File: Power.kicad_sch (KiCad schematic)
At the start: 44 parts, among them SW901 PWR_SW, U901 BQ24075RGT, U902 TPS73733QDRBRQ1, U903 TPS73733QDRBRQ1

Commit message: (sch) change 2.2k R to 0402
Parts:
- R905, R908: footprint Resistor_SMD:R_0603_1608Metric_Pad0.98x0.95mm_HandSolder -> Resistor_SMD:R_0402_1005Metric; MPN RC0603FR-072K2L -> RT0402FRE072K2L
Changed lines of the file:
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@@
       (effects (font (size 1.27 1.27)))
     )
-    (property "Footprint" "Resistor_SMD:R_0603_1608Metric_Pad0.98x0.95mm_HandSolder" (at 79.375 167.64 0)
+    (property "Footprint" "Resistor_SMD:R_0402_1005Metric" (at 79.375 167.64 0)
       (effects (font (size 1.27 1.27)) hide)
     )
@@
       (effects (font (size 1.27 1.27)) hide)
     )
-    (property "MPN" "RC0603FR-072K2L" (at 79.375 167.64 0)
+    (property "MPN" "RT0402FRE072K2L" (at 79.375 167.64 0)
       (effects (font (size 1.27 1.27)) hide)
     )
@@
       (effects (font (size 1.27 1.27)) (justify left))
     )
-    (property "Footprint" "Resistor_SMD:R_0603_1608Metric_Pad0.98x0.95mm_HandSolder" (at 66.04 167.005 0)
+    (property "Footprint" "Resistor_SMD:R_0402_1005Metric" (at 66.04 167.005 0)
       (effects (font (size 1.27 1.27)) hide)
     )
@@
       (effects (font (size 1.27 1.27)) hide)
     )
-    (property "MPN" "RC0603FR-072K2L" (at 66.04 167.005 0)
+    (property "MPN" "RT0402FRE072K2L" (at 66.04 167.005 0)
       (effects (font (size 1.27 1.27)) hide)
     )

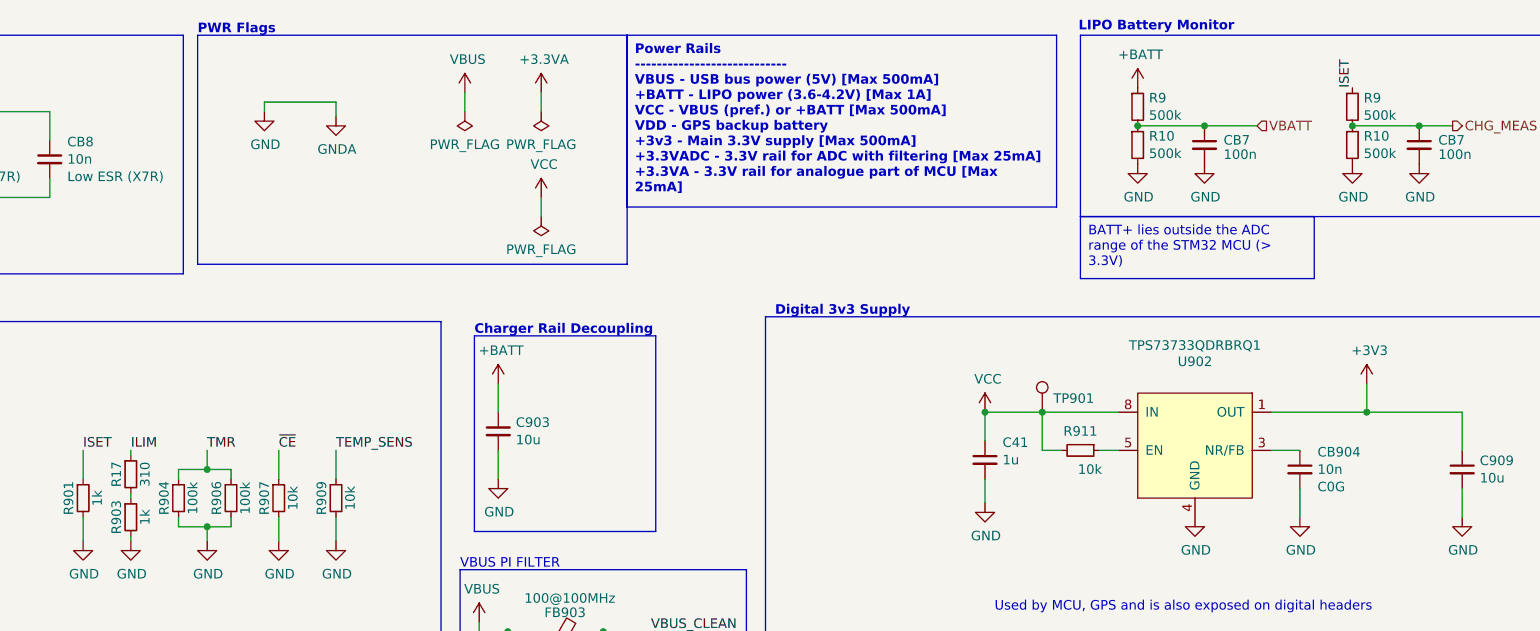
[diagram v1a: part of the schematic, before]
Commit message: (sch) change passives to 0402
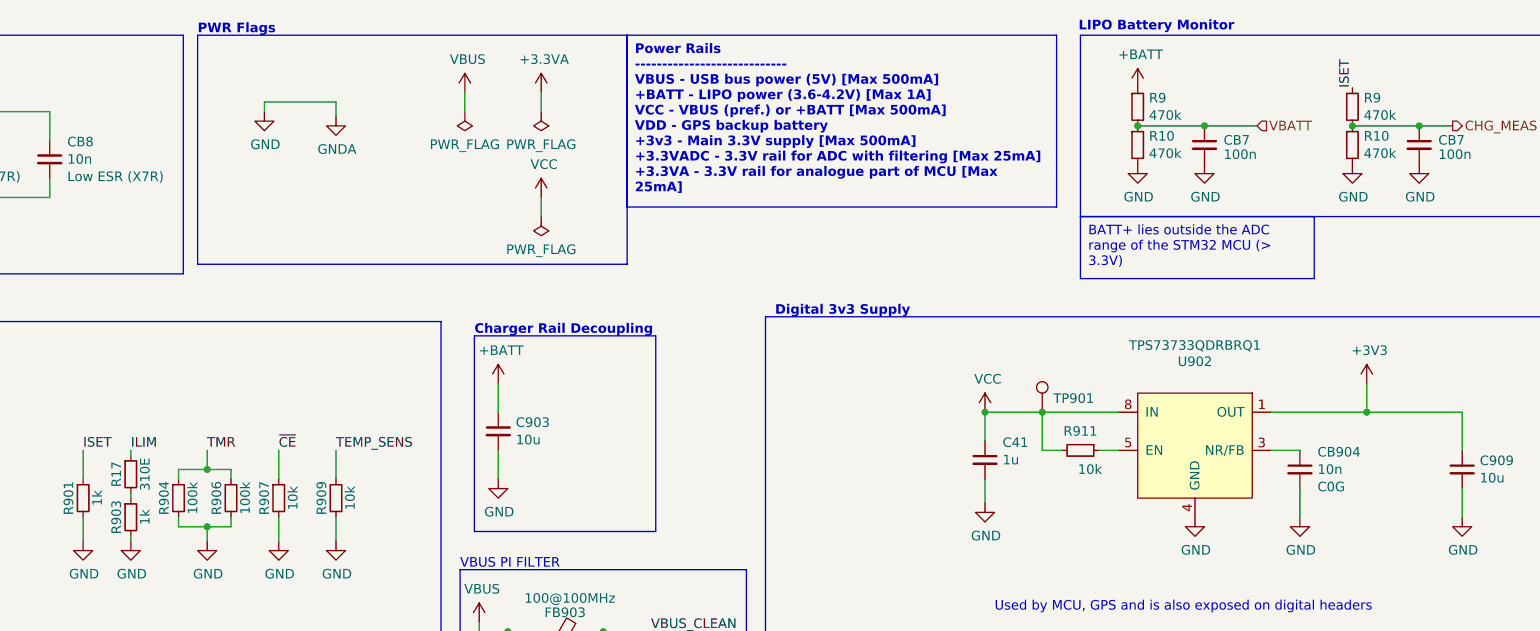
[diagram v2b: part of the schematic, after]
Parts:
- CB8, CB904, CB905: footprint Capacitor_SMD:C_0603_1608Metric_Pad1.08x0.95mm_HandSolder -> Capacitor_SMD:C_0603_1608Metric; MPN C0603C103J5RACTU -> GRM1885C1H103JA01J; Mfr. KEMET -> Murata
- D901, D902: footprint LED_SMD:LED_0603_1608Metric_Pad1.05x0.95mm_HandSolder -> LED_SMD:LED_0603_1608Metric
- R10, R9: value 500k -> 470k; footprint Resistor_SMD:R_0603_1608Metric_Pad0.98x0.95mm_HandSolder -> Resistor_SMD:R_0603_1608Metric
- R17: value 310 -> 310E; footprint Resistor_SMD:R_0603_1608Metric_Pad0.98x0.95mm_HandSolder -> Resistor_SMD:R_0402_1005Metric; MPN ERJ-3EKF3090V -> RT0402FRE07309RL; Mfr. Panasonic -> Yageo
- R901, R903: footprint Resistor_SMD:R_0603_1608Metric_Pad0.98x0.95mm_HandSolder -> Resistor_SMD:R_0402_1005Metric; MPN (none) -> RT0402FRE071KL; Mfr. (none) -> Yageo
- R904, R906, R910: footprint Resistor_SMD:R_0603_1608Metric_Pad0.98x0.95mm_HandSolder -> Resistor_SMD:R_0402_1005Metric; MPN (none) -> RT0402FRE07100KL; Mfr. (none) -> Yageo
- R907, R909, R911, R912: footprint Resistor_SMD:R_0603_1608Metric_Pad0.98x0.95mm_HandSolder -> Resistor_SMD:R_0402_1005Metric; MPN RC0603JR-0710KL -> RT0402FRE1310KL

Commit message: (pcb) initial layout
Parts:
- added R917, R918: 10k, Resistor_SMD:R_0402_1005Metric, symbol Device:R_Small
- CB7: footprint Capacitor_SMD:C_0603_1608Metric_Pad1.08x0.95mm_HandSolder -> Capacitor_SMD:C_0402_1005Metric; MPN C0603C104M5RACTU -> C0402C104K8PACTU
- CB8, CB904, CB905: footprint Capacitor_SMD:C_0603_1608Metric -> Capacitor_SMD:C_0402_1005Metric; MPN GRM1885C1H103JA01J -> C0402C103K3RAC7411; Mfr. Murata -> KEMET
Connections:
- net +BATT: now also JP901.3 (B)
- net CHG_EN1: now also R917.1
- net CHG_EN2: now also R918.1
- net GND: now also R917.2, R918.2
- net VOUT: now also U901.10 (OUT), U901.11 (OUT)
- net V_OVR: now reaches F901.1, JP901.2 (C)
- net PWR_SW: now reaches R910.2, SW901.2 (B)
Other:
- moved on the sheet: R17, R901, R903, R904, R906, R907, R909

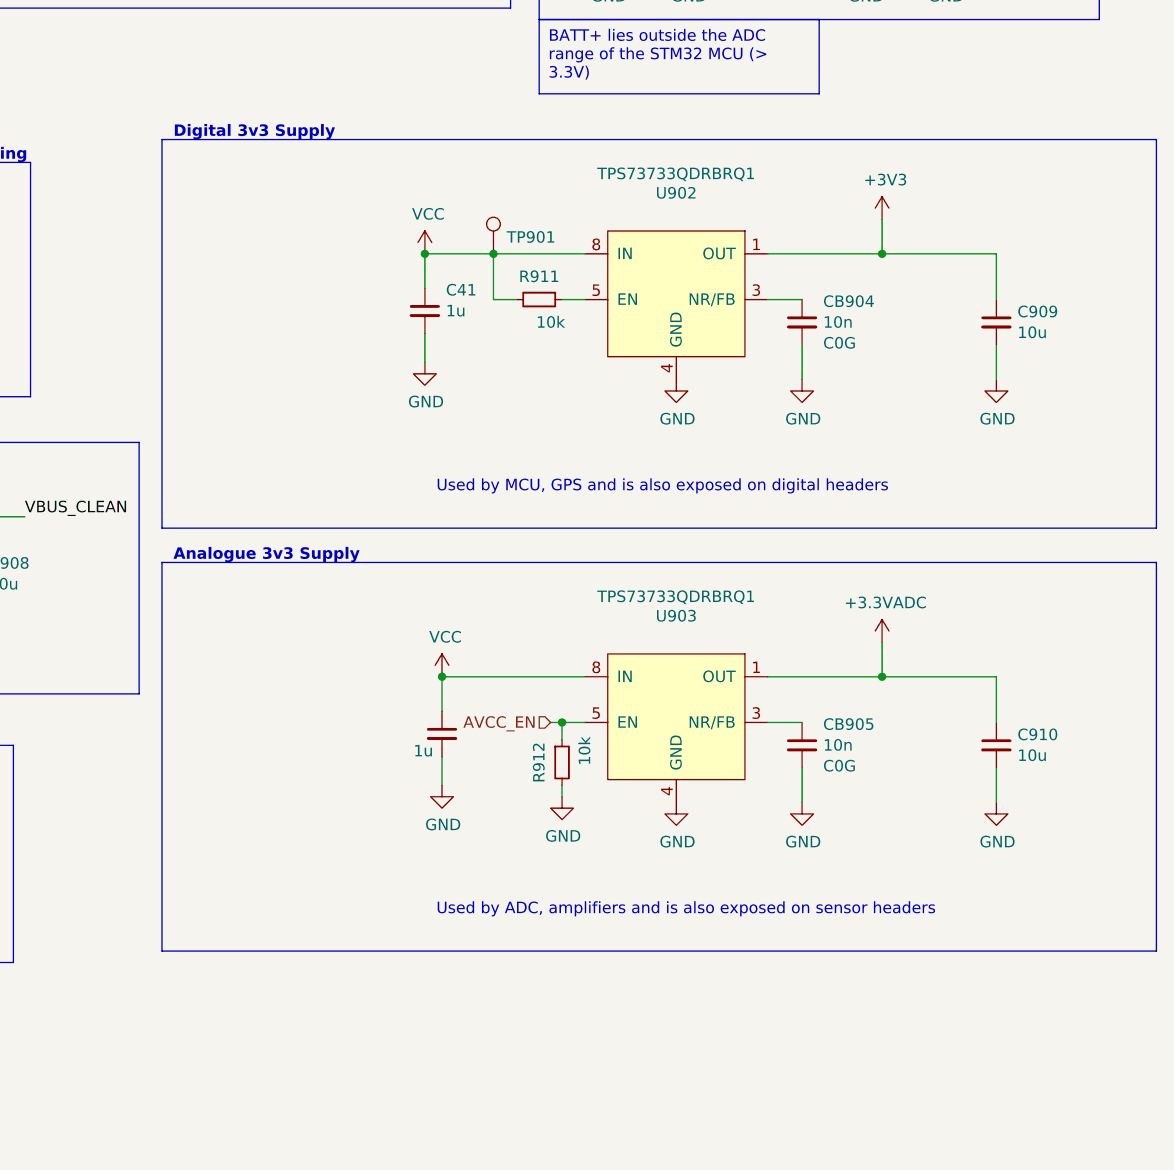
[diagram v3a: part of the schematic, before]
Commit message: (sch) change LDOs
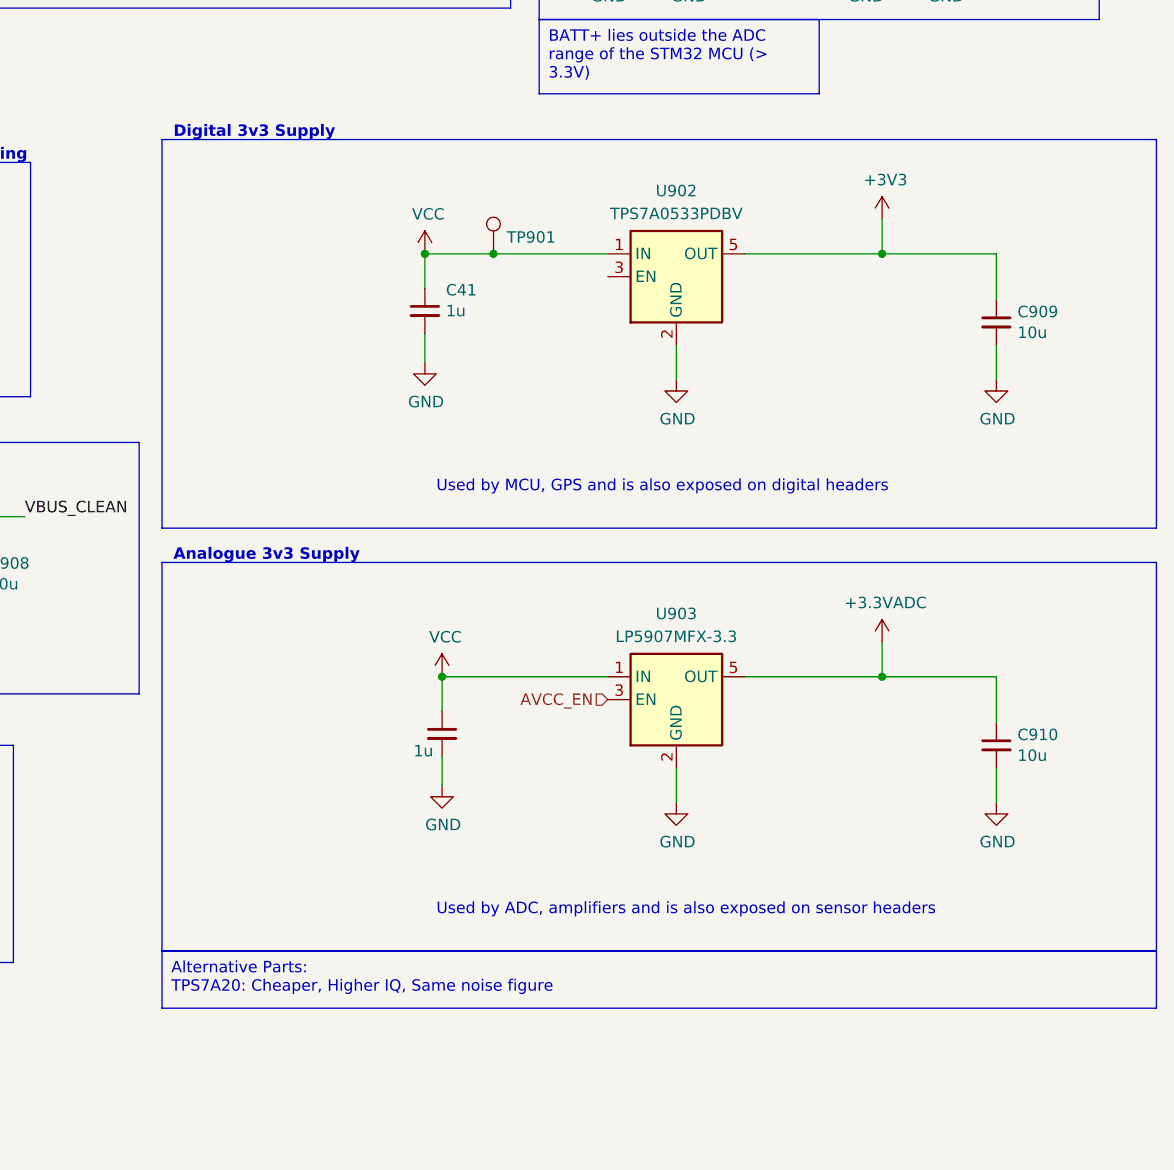
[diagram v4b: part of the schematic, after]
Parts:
- removed CB904, CB905: 10n, Capacitor_SMD:C_0402_1005Metric, symbol Device:C_Small
- removed R911, R912: 10k, Resistor_SMD:R_0402_1005Metric, symbol Device:R_Small
- removed U902, U903: TPS73733QDRBRQ1, grootvoet:Texas_DRB0008A, symbol grootvoet:TPS73733QDRBRQ1
- added U902: TPS7A0533PDBV, Package_TO_SOT_SMD:SOT-23-5, symbol Regulator_Linear:TPS7A0533PDBV
- added U903: LP5907MFX-3.3, Package_TO_SOT_SMD:SOT-23-5, symbol Regulator_Linear:LP5907MFX-3.3
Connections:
- net +3.3VADC: now also U903.5 (OUT)
- net +3V3: now also U902.5 (OUT)
- net AVCC_EN: now also U903.3 (EN)
- net GND: now also U902.2 (GND), U903.2 (GND)
- net VCC: now also U902.1 (IN), U903.1 (IN)

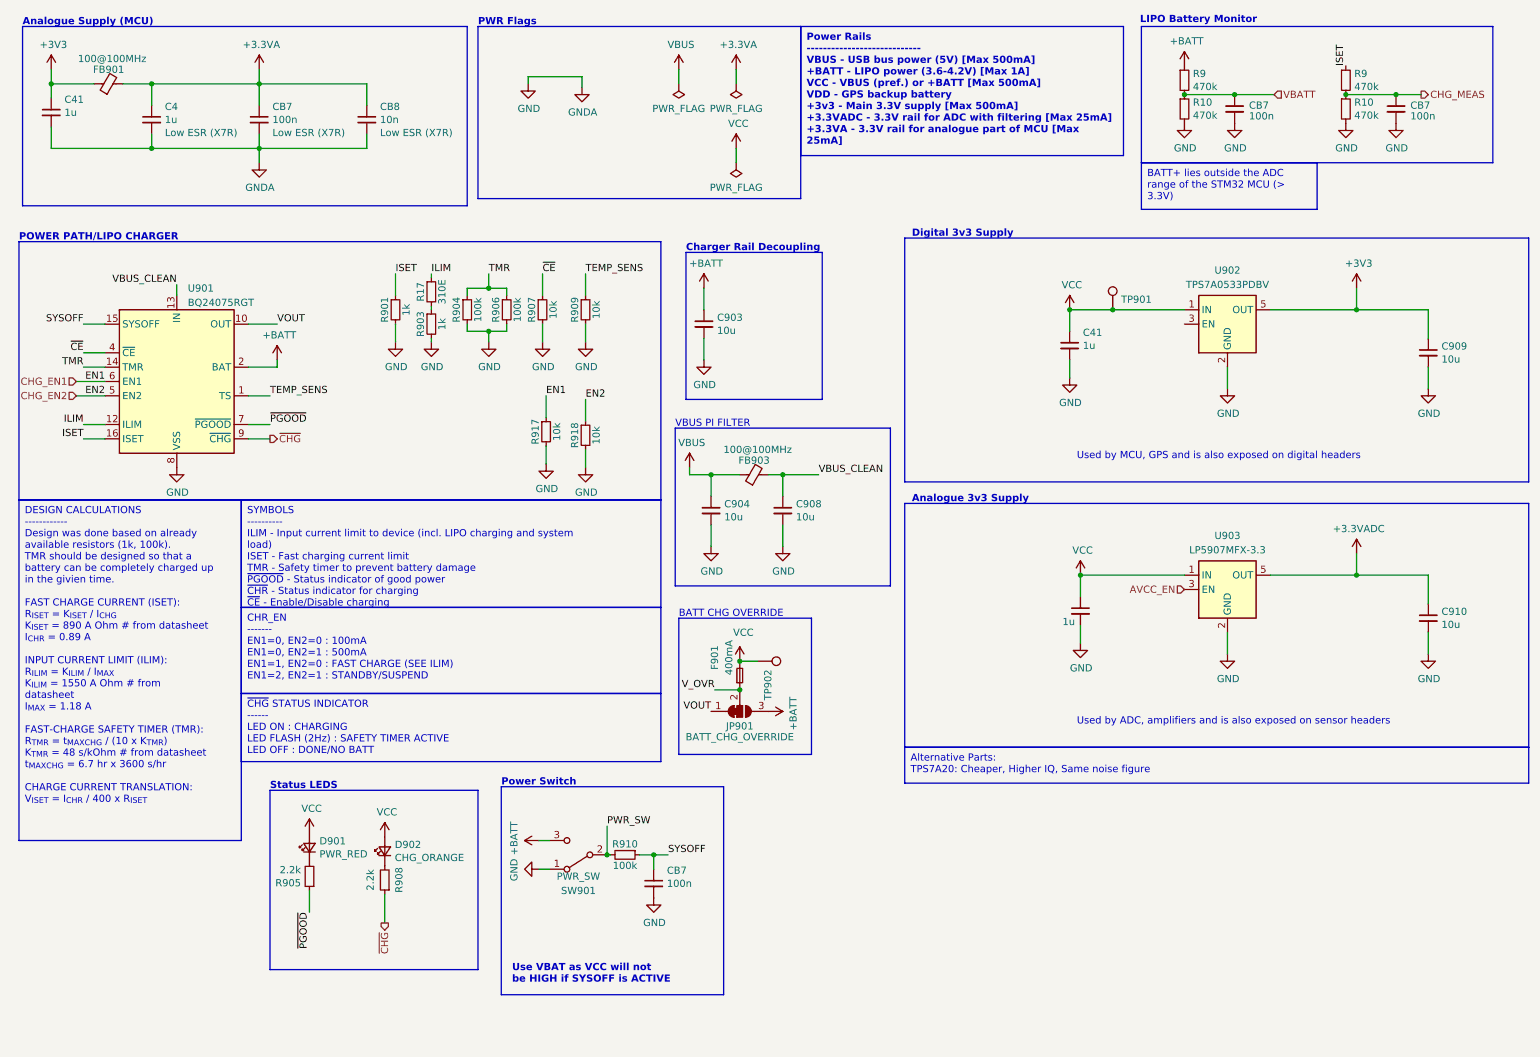
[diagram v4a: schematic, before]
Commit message: (sch) replace PWR SW with DP3T
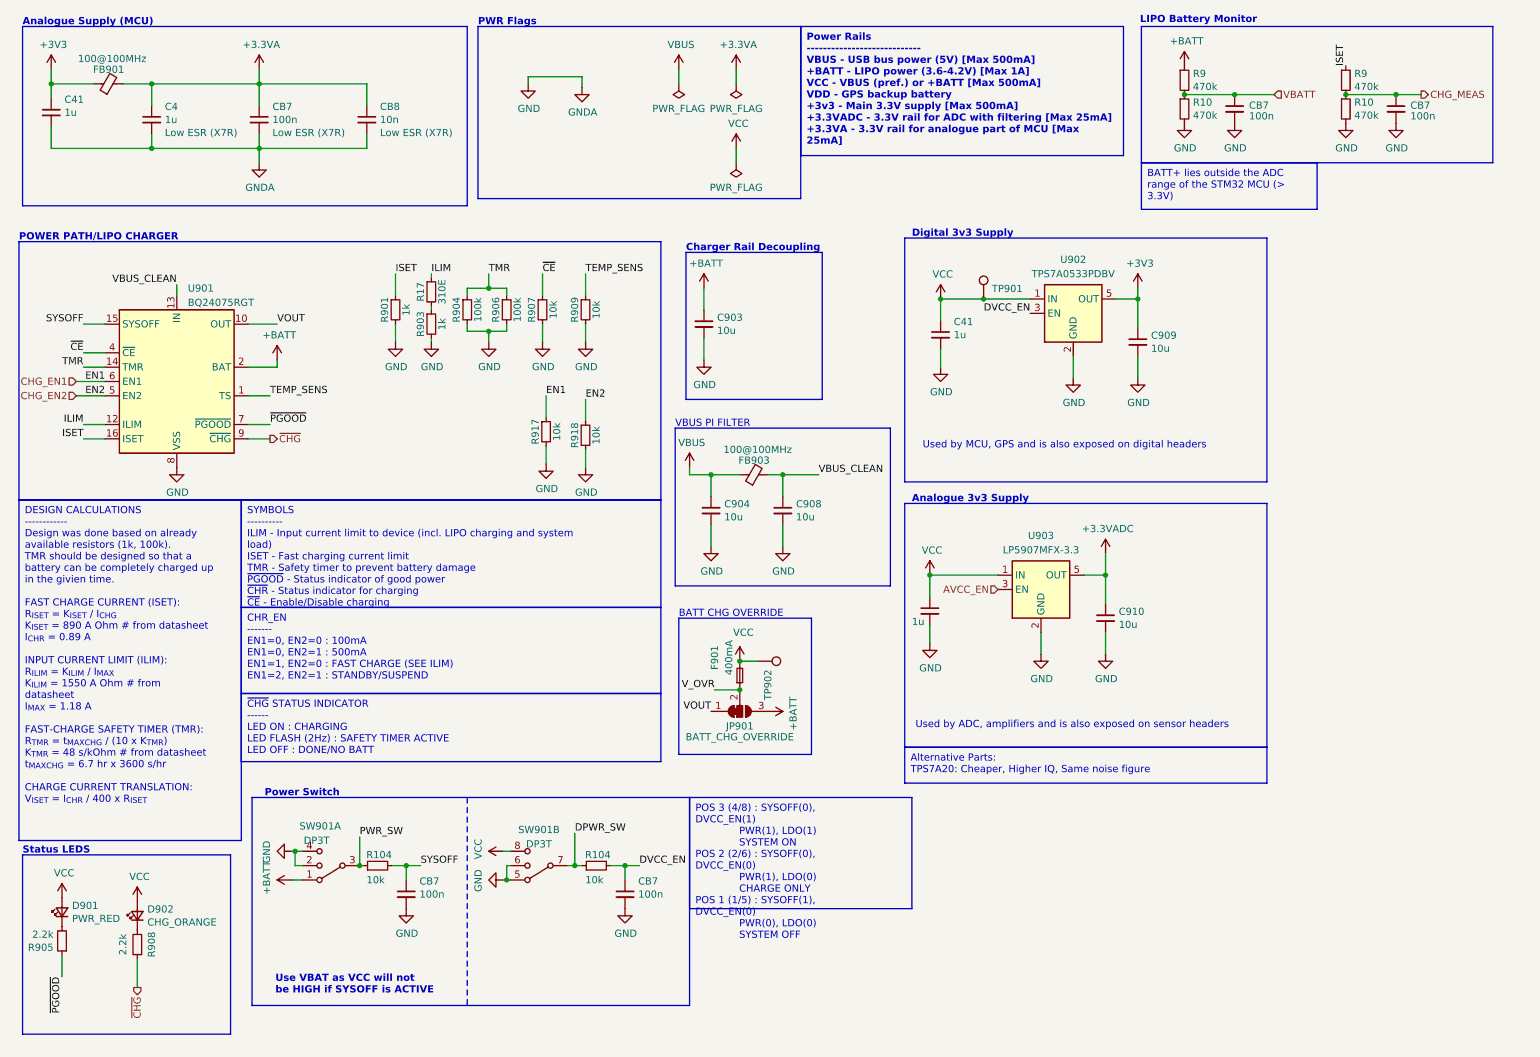
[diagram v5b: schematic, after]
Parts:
- removed R910: 100k, Resistor_SMD:R_0402_1005Metric, symbol Device:R_Small
- removed SW901: PWR_SW, Button_Switch_SMD:SW_SPDT_CK-JS102011SAQN, symbol Switch:SW_SPDT
- added CB7: 100n, Capacitor_SMD:C_0402_1005Metric, symbol Device:C_Small
- added R104 (x2): 10k, Resistor_SMD:R_0402_1005Metric, symbol Device:R_Small
- added SW901: DP3T, grootvoet:SW_DP3T_Nidec-Cobal_CL-SB-23A, symbol Switch:SW_DP3T
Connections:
- net +BATT: now also SW901.1
- net GND: now also CB7.2, SW901.2, SW901.4, SW901.5, SW901.6
- net PWR_SW: now also R104.1, SW901.3
- net SYSOFF: now also R104.2
- net VCC: now also SW901.8
- net DVCC_EN: now reaches U902.3 (EN)
- net DVCC_EN: now also CB7.1, R104.2
- new net DPWR_SW: R104.1, SW901.7
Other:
- moved on the sheet: C41, C909, C910, CB7, D901, D902, R905, R908, TP901, U902, U903

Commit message: (sch) change default charging & add PWR LEDs
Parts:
- added D903: PWR_AVCC, LED_SMD:LED_0603_1608Metric, symbol Device:LED_Small
- added D904: PWR_DVCC, LED_SMD:LED_0603_1608Metric, symbol Device:LED_Small
- added R912: 100k, Resistor_SMD:R_0402_1005Metric, symbol Device:R_Small
- added R919: 2.2k, Resistor_SMD:R_0402_1005Metric, symbol Device:R_Small
- D901: value PWR_RED -> PWR_VBUS
- R917: value 10k -> 100k; MPN RT0402FRE1310KL -> RT0402FRE07100KL
- R918: value 10k -> 2.2k; MPN RT0402FRE1310KL -> RT0402FRE072K2L
- U901: value BQ24075RGT -> BQ24075; MPN (none) -> BQ24075TRGTR; Mfr. (none) -> Texas Instruments
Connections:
- net +3.3VADC: now also D903.2 (A)
- net +3V3: now also D904.2 (A)
- net CHG_EN1: now also R912.1; no longer R917.1
- net CHG_EN2: now also R917.1; no longer R918.1
- net GND: now also R918.1, R919.1; no longer R918.2
- net VCC: now also R912.2
- new net: D903.1 (K), R918.2
- new net: D904.1 (K), R919.2
